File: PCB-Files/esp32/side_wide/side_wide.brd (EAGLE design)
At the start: 50 x 17 mm, 5 parts

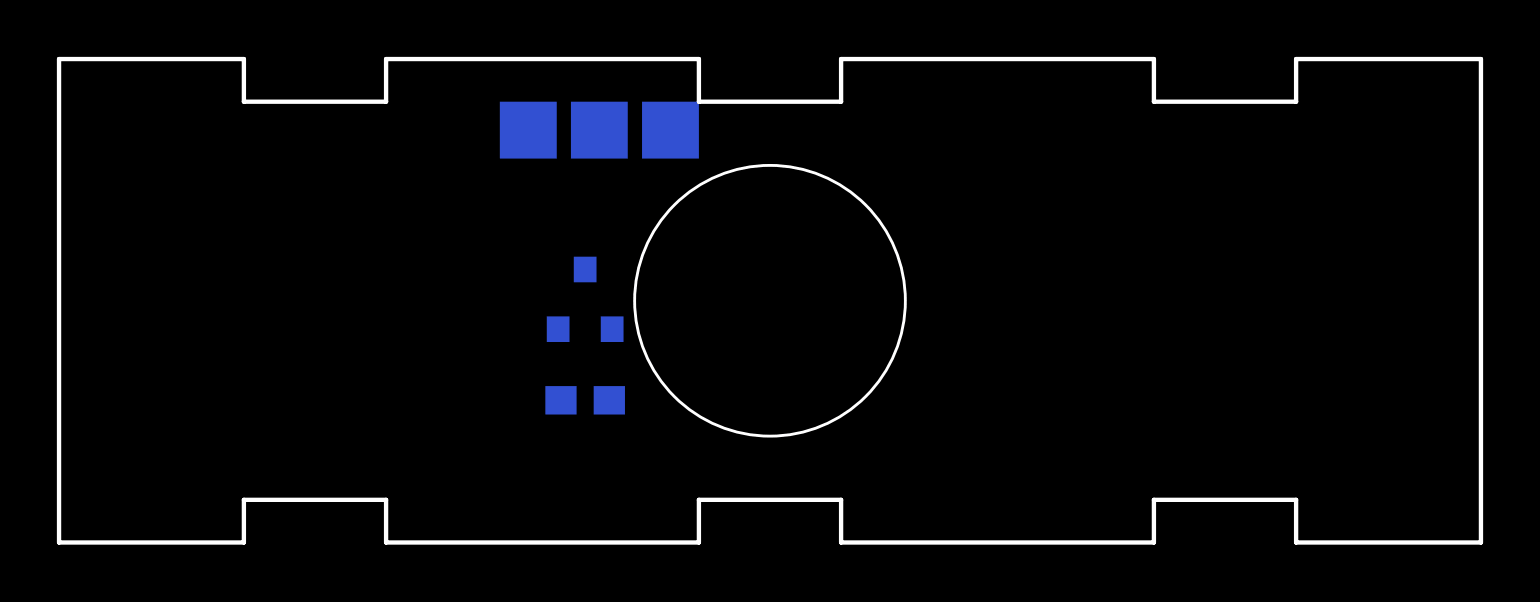
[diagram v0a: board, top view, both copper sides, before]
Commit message: basic layout; dimension for toothed joints
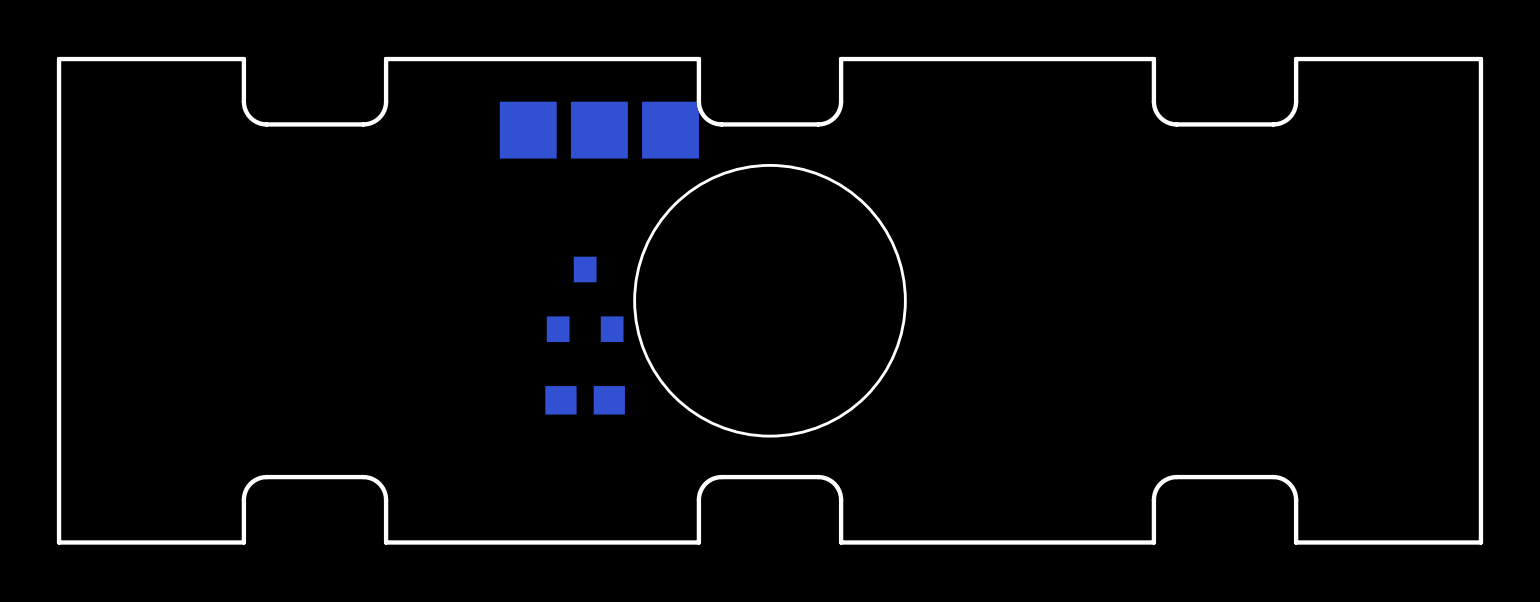
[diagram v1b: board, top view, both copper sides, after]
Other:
- outline, holes or cut-outs redrawn
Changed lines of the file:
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@@
 <setting verticaltext="up"/>
 </settings>
-<grid distance="0.5" unitdist="mm" unit="mm" style="lines" multiple="1" display="yes" altdistance="0.025" altunitdist="inch" altunit="inch"/>
+<grid distance="0.1" unitdist="mm" unit="mm" style="lines" multiple="1" display="yes" altdistance="0.025" altunitdist="inch" altunit="inch"/>
 <layers>
 <layer number="1" name="Top" color="4" fill="1" visible="yes" active="yes"/>
@@
 <board>
 <plain>
-<wire x1="50" y1="0" x2="43.5" y2="0" width="0.1524" layer="20"/>
-<wire x1="38.5" y1="0" x2="27.5" y2="0" width="0.1524" layer="20"/>
-<wire x1="22.5" y1="0" x2="11.5" y2="0" width="0.1524" layer="20"/>
-<wire x1="6.5" y1="0" x2="0" y2="0" width="0.1524" layer="20"/>
 <circle x="25" y="8.5" radius="4.76" width="0.1" layer="20"/>
-<wire x1="6.5" y1="0" x2="6.5" y2="1.5" width="0.1524" layer="20"/>
-<wire x1="6.5" y1="1.5" x2="11.5" y2="1.5" width="0.1524" layer="20"/>
-<wire x1="11.5" y1="1.5" x2="11.5" y2="0" width="0.1524" layer="20"/>
-<wire x1="22.5" y1="1.5" x2="27.5" y2="1.5" width="0.1524" layer="20"/>
-<wire x1="38.5" y1="1.5" x2="43.5" y2="1.5" width="0.1524" layer="20"/>
-<wire x1="22.5" y1="1.5" x2="22.5" y2="0" width="0.1524" layer="20"/>
-<wire x1="27.5" y1="1.5" x2="27.5" y2="0" width="0.1524" layer="20"/>
-<wire x1="38.5" y1="1.5" x2="38.5" y2="0" width="0.1524" layer="20"/>
-<wire x1="43.5" y1="1.5" x2="43.5" y2="0" width="0.1524" layer="20"/>
 <dimension x1="0" y1="0" x2="50" y2="0" x3="25" y3="-3.25" textsize="1.778" layer="47"/>
-<wire x1="0" y1="17" x2="6.5" y2="17" width="0.1524" layer="20"/>
-<wire x1="11.5" y1="17" x2="22.5" y2="17" width="0.1524" layer="20"/>
-<wire x1="27.5" y1="17" x2="38.5" y2="17" width="0.1524" layer="20"/>
-<wire x1="43.5" y1="17" x2="50" y2="17" width="0.1524" layer="20"/>
-<wire x1="43.5" y1="17" x2="43.5" y2="15.5" width="0.1524" layer="20"/>
-<wire x1="43.5" y1="15.5" x2="38.5" y2="15.5" width="0.1524" layer="20"/>
-<wire x1="38.5" y1="15.5" x2="38.5" y2="17" width="0.1524" layer="20"/>
-<wire x1="27.5" y1="15.5" x2="22.5" y2="15.5" width="0.1524" layer="20"/>
-<wire x1="11.5" y1="15.5" x2="6.5" y2="15.5" width="0.1524" layer="20"/>
-<wire x1="27.5" y1="15.5" x2="27.5" y2="17" width="0.1524" layer="20"/>
-<wire x1="22.5" y1="15.5" x2="22.5" y2="17" width="0.1524" layer="20"/>
-<wire x1="11.5" y1="15.5" x2="11.5" y2="17" width="0.1524" layer="20"/>
-<wire x1="6.5" y1="15.5" x2="6.5" y2="17" width="0.1524" layer="20"/>
 <wire x1="0" y1="17" x2="0" y2="0" width="0.1524" layer="20"/>
 <wire x1="50" y1="17" x2="50" y2="0" width="0.1524" layer="20"/>
 <dimension x1="50" y1="17" x2="50" y2="0" x3="59.5" y3="8.5" textsize="1.778" layer="47"/>
-<dimension x1="43.5" y1="15.5" x2="43.5" y2="1.5" x3="54.5" y3="8.5" textsize="1.778" layer="47"/>
+<dimension x1="43.5" y1="14.7" x2="43.5" y2="2.3" x3="54.5" y3="8.5" textsize="1.778" layer="47"/>
+<wire x1="7.3" y1="14.7" x2="10.7" y2="14.7" width="0.1524" layer="20"/>
+<wire x1="38.5" y1="17" x2="27.5" y2="17" width="0.1524" layer="20"/>
+<wire x1="27.5" y1="17" x2="27.5" y2="15.5" width="0.1524" layer="20"/>
+<wire x1="22.5" y1="17" x2="11.5" y2="17" width="0.1524" layer="20"/>
+<wire x1="6.5" y1="17" x2="0" y2="17" width="0.1524" layer="20"/>
+<wire x1="11.5" y1="17" x2="11.5" y2="15.5" width="0.1524" layer="20"/>
+<wire x1="6.5" y1="17" x2="6.5" y2="15.5" width="0.1524" layer="20"/>
+<wire x1="26.7" y1="14.7" x2="27.5" y2="15.5" width="0.1524" layer="20" curve="90"/>
+<wire x1="10.7" y1="14.7" x2="11.5" y2="15.5" width="0.1524" layer="20" curve="90"/>
+<wire x1="6.5" y1="15.5" x2="7.3" y2="14.7" width="0.1524" layer="20" curve="90"/>
+<wire x1="22.5" y1="17" x2="22.5" y2="15.5" width="0.1524" layer="20"/>
+<wire x1="22.5" y1="15.5" x2="23.3" y2="14.7" width="0.1524" layer="20" curve="90"/>
+<wire x1="23.3" y1="14.7" x2="26.7" y2="14.7" width="0.1524" layer="20"/>
+<wire x1="38.5" y1="17" x2="38.5" y2="15.5" width="0.1524" layer="20"/>
+<wire x1="38.5" y1="15.5" x2="39.3" y2="14.7" width="0.1524" layer="20" curve="90"/>
+<wire x1="50" y1="17" x2="43.5" y2="17" width="0.1524" layer="20"/>
+<wire x1="43.5" y1="17" x2="43.5" y2="15.5" width="0.1524" layer="20"/>
+<wire x1="42.7" y1="14.7" x2="43.5" y2="15.5" width="0.1524" layer="20" curve="90"/>
+<wire x1="39.3" y1="14.7" x2="42.7" y2="14.7" width="0.1524" layer="20"/>
+<wire x1="42.7" y1="2.3" x2="39.3" y2="2.3" width="0.1524" layer="20"/>
+<wire x1="11.5" y1="0" x2="22.5" y2="0" width="0.1524" layer="20"/>
+<wire x1="22.5" y1="0" x2="22.5" y2="1.5" width="0.1524" layer="20"/>
+<wire x1="27.5" y1="0" x2="38.5" y2="0" width="0.1524" layer="20"/>
+<wire x1="43.5" y1="0" x2="50" y2="0" width="0.1524" layer="20"/>
+<wire x1="38.5" y1="0" x2="38.5" y2="1.5" width="0.1524" layer="20"/>
+<wire x1="43.5" y1="0" x2="43.5" y2="1.5" width="0.1524" layer="20"/>
+<wire x1="23.3" y1="2.3" x2="22.5" y2="1.5" width="0.1524" layer="20" curve="90"/>
+<wire x1="39.3" y1="2.3" x2="38.5" y2="1.5" width="0.1524" layer="20" curve="90"/>
+<wire x1="43.5" y1="1.5" x2="42.7" y2="2.3" width="0.1524" layer="20" curve="90"/>
+<wire x1="27.5" y1="0" x2="27.5" y2="1.5" width="0.1524" layer="20"/>
+<wire x1="27.5" y1="1.5" x2="26.7" y2="2.3" width="0.1524" layer="20" curve="90"/>
+<wire x1="26.7" y1="2.3" x2="23.3" y2="2.3" width="0.1524" layer="20"/>
+<wire x1="11.5" y1="0" x2="11.5" y2="1.5" width="0.1524" layer="20"/>
+<wire x1="11.5" y1="1.5" x2="10.7" y2="2.3" width="0.1524" layer="20" curve="90"/>
+<wire x1="0" y1="0" x2="6.5" y2="0" width="0.1524" layer="20"/>
+<wire x1="6.5" y1="0" x2="6.5" y2="1.5" width="0.1524" layer="20"/>
+<wire x1="7.3" y1="2.3" x2="6.5" y2="1.5" width="0.1524" layer="20" curve="90"/>
+<wire x1="10.7" y1="2.3" x2="7.3" y2="2.3" width="0.1524" layer="20"/>
 </plain>
 <attributes>
